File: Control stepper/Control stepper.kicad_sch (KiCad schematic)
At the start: 3 parts, among them Q1 2n2222a

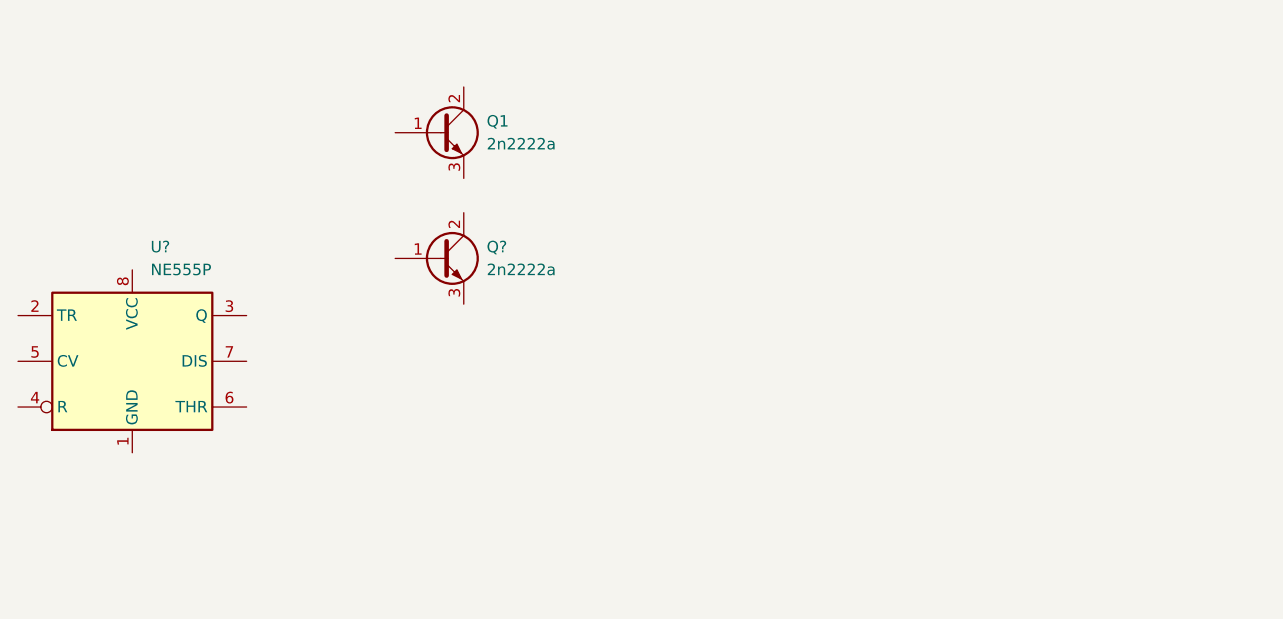
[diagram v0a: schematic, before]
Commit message: Añadida carpeta de código de arduino
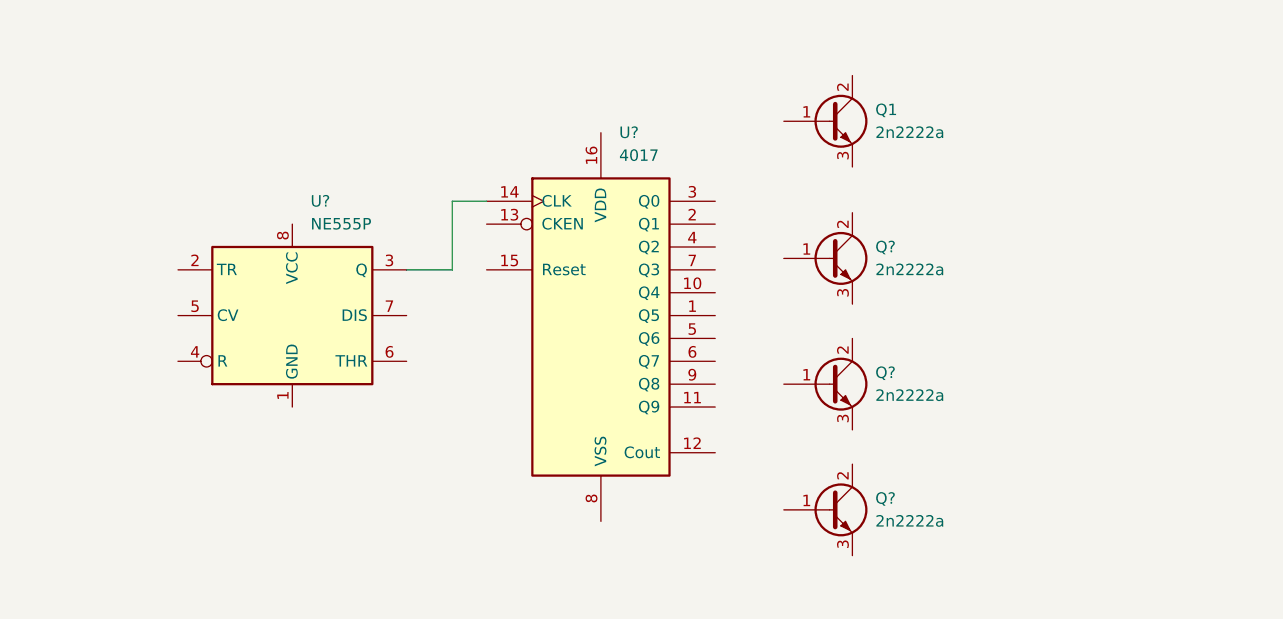
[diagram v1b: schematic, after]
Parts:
- added Q? (x2): 2n2222a, Package_TO_SOT_THT:TO-3PB-3_Vertical, symbol Transistor_BJT:2SD1047
- added U?: 4017, symbol 4xxx:4017
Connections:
- net at U?.3 (Q): now also U?.14 (CLK)
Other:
- moved on the sheet: Q1, Q?, U?
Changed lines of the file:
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@@
 (kicad_sch (version 20211123) (generator eeschema)
   (paper "A4")
-  (symbol (lib_id "Timer:NE555P") (at 64.77 109.22 0) (unit 1)
+  (wire (pts (xy 100.33 99.06) (xy 100.33 91.44))
+    (stroke (width 0) (type default) (color 0 0 0 0))
+  )
+  (wire (pts (xy 100.33 91.44) (xy 104.14 91.44))
+    (stroke (width 0) (type default) (color 0 0 0 0))
+  )
+  (wire (pts (xy 95.25 99.06) (xy 100.33 99.06))
+    (stroke (width 0) (type default) (color 0 0 0 0))
+  )
+  (symbol (lib_id "Timer:NE555P") (at 82.55 104.14 0) (unit 1)
     (in_bom yes) (on_board yes) (fields_autoplaced)
-    (property "Reference" "U?" (id 0) (at 66.7894 96.52 0)
+    (property "Reference" "U?" (id 0) (at 84.5694 91.44 0)
       (effects (font (size 1.27 1.27)) (justify left))
     )
-    (property "Value" "NE555P" (id 1) (at 66.7894 99.06 0)
+    (property "Value" "NE555P" (id 1) (at 84.5694 93.98 0)
       (effects (font (size 1.27 1.27)) (justify left))
     )
-    (property "Footprint" "Package_DIP:DIP-8_W7.62mm" (id 2) (at 81.28 119.38 0)
+    (property "Footprint" "Package_DIP:DIP-8_W7.62mm" (id 2) (at 99.06 114.3 0)
       (effects (font (size 1.27 1.27)) hide)
     )
-    (property "Datasheet" "http://www.ti.com/lit/ds/symlink/ne555.pdf" (id 3) (at 86.36 119.38 0)
+    (property "Datasheet" "http://www.ti.com/lit/ds/symlink/ne555.pdf" (id 3) (at 104.14 114.3 0)
       (effects (font (size 1.27 1.27)) hide)
     )
@@
     (pin "7")
   )
-  (symbol (lib_id "Transistor_BJT:2SD1047") (at 99.06 97.79 0) (unit 1)
+  (symbol (lib_id "Transistor_BJT:2SD1047") (at 142.24 111.76 0) (unit 1)
     (in_bom yes) (on_board yes) (fields_autoplaced)
-    (property "Reference" "Q?" (id 0) (at 104.14 96.5199 0)
+    (property "Reference" "Q?" (id 0) (at 147.32 110.4899 0)
       (effects (font (size 1.27 1.27)) (justify left))
     )
-    (property "Value" "2n2222a" (id 1) (at 104.14 99.0599 0)
+    (property "Value" "2n2222a" (id 1) (at 147.32 113.0299 0)
       (effects (font (size 1.27 1.27)) (justify left))
     )
-    (property "Footprint" "Package_TO_SOT_THT:TO-3PB-3_Vertical" (id 2) (at 105.41 99.695 0)
+    (property "Footprint" "Package_TO_SOT_THT:TO-3PB-3_Vertical" (id 2) (at 148.59 113.665 0)
       (effects (font (size 1.27 1.27) italic) (justify left) hide)
     )
-    (property "Datasheet" "http://www.st.com/resource/en/datasheet/2sd1047.pdf" (id 3) (at 99.06 97.79 0)
+    (property "Datasheet" "http://www.st.com/resource/en/datasheet/2sd1047.pdf" (id 3) (at 142.24 111.76 0)
       (effects (font (size 1.27 1.27)) (justify left) hide)
     )
@@
     (pin "3")
   )
-  (symbol (lib_id "Transistor_BJT:2SD1047") (at 99.06 83.82 0) (unit 1)
+  (symbol (lib_id "Transistor_BJT:2SD1047") (at 142.24 125.73 0) (unit 1)
     (in_bom yes) (on_board yes) (fields_autoplaced)
-    (property "Reference" "Q1" (id 0) (at 104.14 82.5499 0)
+    (property "Reference" "Q?" (id 0) (at 147.32 124.4599 0)
       (effects (font (size 1.27 1.27)) (justify left))
     )
-    (property "Value" "2n2222a" (id 1) (at 104.14 85.0899 0)
+    (property "Value" "2n2222a" (id 1) (at 147.32 126.9999 0)
       (effects (font (size 1.27 1.27)) (justify left))
     )
-    (property "Footprint" "Package_TO_SOT_THT:TO-3PB-3_Vertical" (id 2) (at 105.41 85.725 0)
+    (property "Footprint" "Package_TO_SOT_THT:TO-3PB-3_Vertical" (id 2) (at 148.59 127.635 0)
       (effects (font (size 1.27 1.27) italic) (justify left) hide)
     )
-    (property "Datasheet" "http://www.st.com/resource/en/datasheet/2sd1047.pdf" (id 3) (at 99.06 83.82 0)
+    (property "Datasheet" "http://www.st.com/resource/en/datasheet/2sd1047.pdf" (id 3) (at 142.24 125.73 0)
       (effects (font (size 1.27 1.27)) (justify left) hide)
     )
@@
     (pin "2")
     (pin "3")
+  )
+  (symbol (lib_id "Transistor_BJT:2SD1047") (at 142.24 97.79 0) (unit 1)
+    (in_bom yes) (on_board yes) (fields_autoplaced)
+    (property "Reference" "Q?" (id 0) (at 147.32 96.5199 0)
+      (effects (font (size 1.27 1.27)) (justify left))
+    )
+    (property "Value" "2n2222a" (id 1) (at 147.32 99.0599 0)
+      (effects (font (size 1.27 1.27)) (justify left))
+    )
+    (property "Footprint" "Package_TO_SOT_THT:TO-3PB-3_Vertical" (id 2) (at 148.59 99.695 0)
+      (effects (font (size 1.27 1.27) italic) (justify left) hide)
+    )
+    (property "Datasheet" "http://www.st.com/resource/en/datasheet/2sd1047.pdf" (id 3) (at 142.24 97.79 0)
+      (effects (font (size 1.27 1.27)) (justify left) hide)
+    )
+    (pin "1")
+    (pin "2")
+    (pin "3")
+  )
+  (symbol (lib_id "Transistor_BJT:2SD1047") (at 142.24 82.55 0) (unit 1)
+    (in_bom yes) (on_board yes) (fields_autoplaced)
+    (property "Reference" "Q1" (id 0) (at 147.32 81.2799 0)
+      (effects (font (size 1.27 1.27)) (justify left))
+    )
+    (property "Value" "2n2222a" (id 1) (at 147.32 83.8199 0)
+      (effects (font (size 1.27 1.27)) (justify left))
+    )
+    (property "Footprint" "Package_TO_SOT_THT:TO-3PB-3_Vertical" (id 2) (at 148.59 84.455 0)
+      (effects (font (size 1.27 1.27) italic) (justify left) hide)
+    )
+    (property "Datasheet" "http://www.st.com/resource/en/datasheet/2sd1047.pdf" (id 3) (at 142.24 82.55 0)
+      (effects (font (size 1.27 1.27)) (justify left) hide)
+    )
+    (pin "1")
+    (pin "2")
+    (pin "3")
+  )
+  (symbol (lib_id "4xxx:4017") (at 116.84 104.14 0) (unit 1)
+    (in_bom yes) (on_board yes) (fields_autoplaced)
+    (property "Reference" "U?" (id 0) (at 118.8594 83.82 0)
+      (effects (font (size 1.27 1.27)) (justify left))
+    )
+    (property "Value" "4017" (id 1) (at 118.8594 86.36 0)
+      (effects (font (size 1.27 1.27)) (justify left))
+    )
+    (property "Footprint" "" (id 2) (at 116.84 104.14 0)
+      (effects (font (size 1.27 1.27)) hide)
+    )
+    (property "Datasheet" "http://www.intersil.com/content/dam/Intersil/documents/cd40/cd4017bms-22bms.pdf" (id 3) (at 116.84 104.14 0)
+      (effects (font (size 1.27 1.27)) hide)
+    )
+    (pin "1")
+    (pin "10")
+    (pin "11")
+    (pin "12")
+    (pin "13")
+    (pin "14")
+    (pin "15")
+    (pin "16")
+    (pin "2")
+    (pin "3")
+    (pin "4")
+    (pin "5")
+    (pin "6")
+    (pin "7")
+    (pin "8")
+    (pin "9")
   )
   (sheet_instances
@@
       (reference "Q1") (unit 1) (value "2n2222a") (footprint "Package_TO_SOT_THT:TO-3PB-3_Vertical")
     )
+    (path "/2ce3dcaa-64a4-4ec7-925e-cda34a695a36"
+      (reference "Q?") (unit 1) (value "2n2222a") (footprint "Package_TO_SOT_THT:TO-3PB-3_Vertical")
+    )
+    (path "/2eec7807-2036-42a0-b763-d8d7931d6a94"
+      (reference "Q?") (unit 1) (value "2n2222a") (footprint "Package_TO_SOT_THT:TO-3PB-3_Vertical")
+    )
     (path "/383e22ae-7025-40ad-b4cf-dc8861149b49"
       (reference "Q?") (unit 1) (value "2n2222a") (footprint "Package_TO_SOT_THT:TO-3PB-3_Vertical")
@@
       (reference "U?") (unit 1) (value "NE555P") (footprint "Package_DIP:DIP-8_W7.62mm")
     )
+    (path "/97b177ea-de0c-48c8-bcee-9dde2dbdcc6f"
+      (reference "U?") (unit 1) (value "4017") (footprint "")
+    )
   )

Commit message: Terminado esquemático del stepper,falta el generador de pulsos
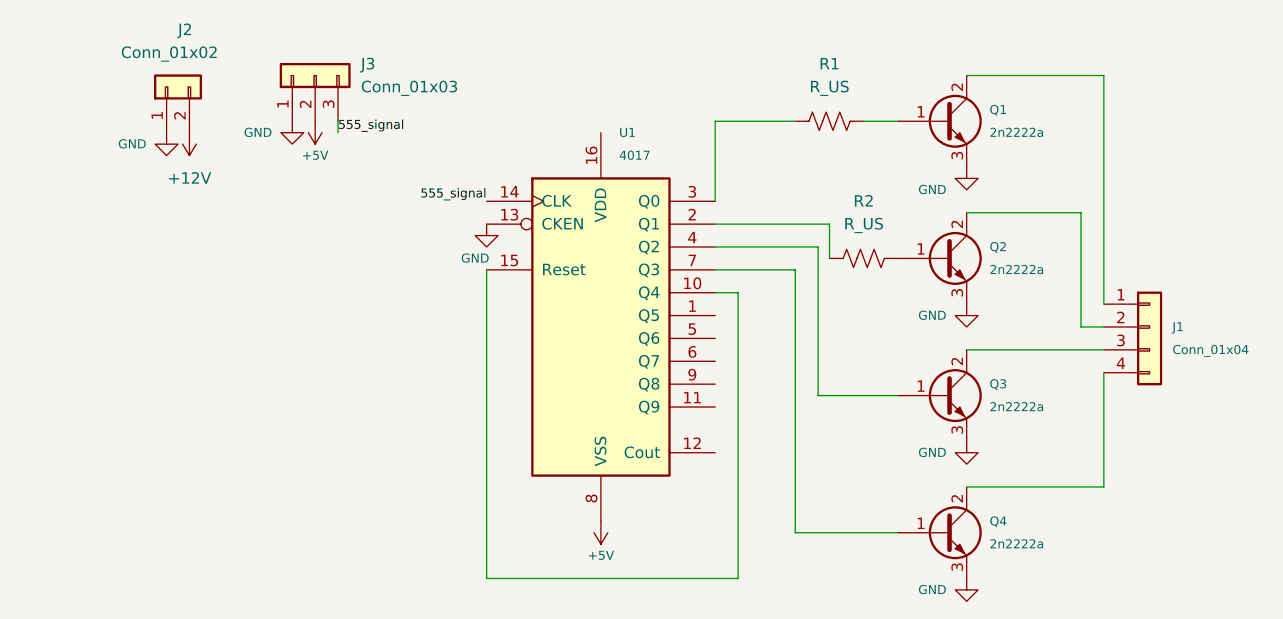
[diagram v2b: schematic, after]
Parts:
- removed U?: NE555P, Package_DIP:DIP-8_W7.62mm, symbol Timer:NE555P
- added J1: Conn_01x04, TerminalBlock:TerminalBlock_bornier-4_P5.08mm, symbol Connector_Generic:Conn_01x04
- added J2: Conn_01x02, TerminalBlock:TerminalBlock_bornier-2_P5.08mm, symbol Connector_Generic:Conn_01x02
- added J3: Conn_01x03, TerminalBlock:TerminalBlock_bornier-3_P5.08mm, symbol Connector_Generic:Conn_01x03
- added R1, R2: R_US, Resistor_THT:R_Axial_DIN0207_L6.3mm_D2.5mm_P15.24mm_Horizontal, symbol Device:R_US
- U1: renamed from U?; footprint (none) -> Package_DIP:DIP-16_W7.62mm_Socket_LongPads
- gave numbers to parts that had none: 3
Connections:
- net 555_signal: now reaches U1.14 (CLK)
- net 555_signal: now also J3.3 (Pin_3)
- net at Q3.1 (B): now also U1.4 (Q2)
- net at Q3.2 (C): now also J1.3 (Pin_3)
- net GND: now reaches Q3.3 (E)
- net GND: now also Q1.3 (E), Q2.3 (E), Q4.3 (E), U1.13 (CKEN), J2.1 (Pin_1), J3.1 (Pin_1)
- net at Q4.1 (B): now also U1.7 (Q3)
- net at Q4.2 (C): now also J1.4 (Pin_4)
- net at Q2.1 (B): now also R2.1
- net at Q2.2 (C): now also J1.2 (Pin_2)
- net at Q1.1 (B): now also R1.1
- net at Q1.2 (C): now also J1.1 (Pin_1)
- net at U1.10 (Q4): now also U1.15 (Reset)
- net at U1.2 (Q1): now also R2.2
- net at U1.3 (Q0): now also R1.2
- net +5V: now reaches U1.8 (VSS)
- net +5V: now also J3.2 (Pin_2)
- new net +12V: J2.2 (Pin_2)
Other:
- moved on the sheet: Q1, Q2, Q3, Q4

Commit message: 3D casi completo falta la pata de abajo
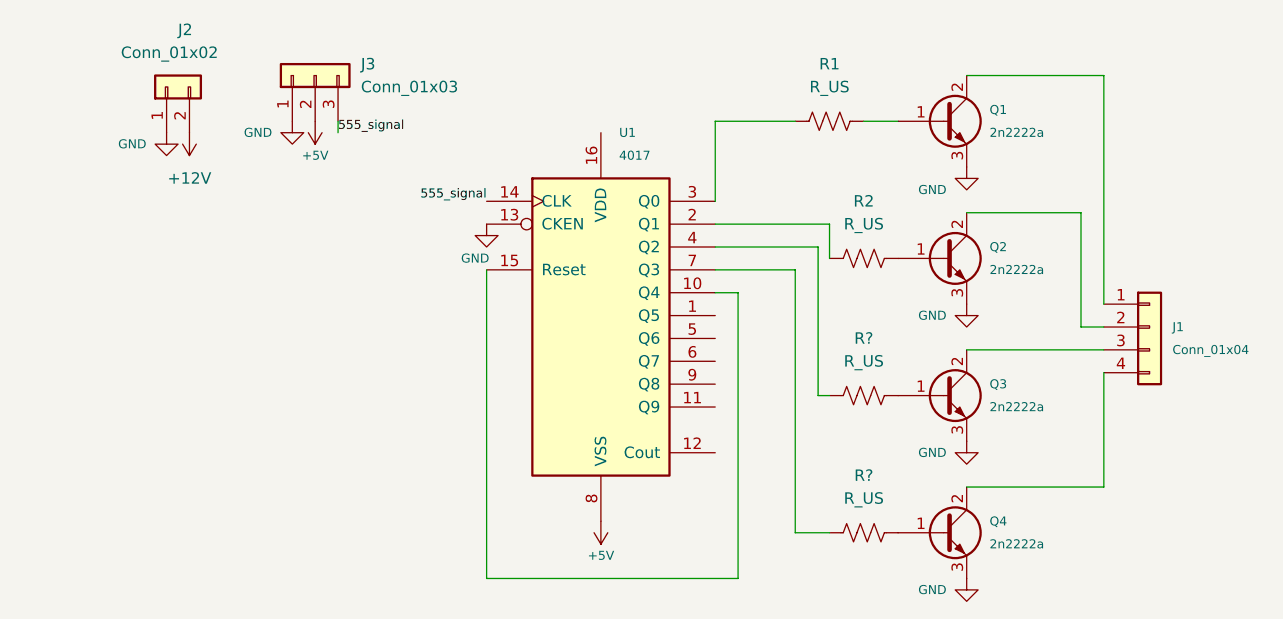
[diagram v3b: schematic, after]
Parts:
- added R? (x2): R_US, Resistor_THT:R_Axial_DIN0207_L6.3mm_D2.5mm_P15.24mm_Horizontal, symbol Device:R_US
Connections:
- net at Q3.1 (B): now also R?.1; no longer U1.4 (Q2)
- net at Q4.1 (B): now also R?.1; no longer U1.7 (Q3)
- new net: R?.2, U1.7 (Q3)
- new net: R?.2, U1.4 (Q2)
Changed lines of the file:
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@@
     (stroke (width 0) (type default) (color 0 0 0 0))
   )
-  (wire (pts (xy 140.97 113.03) (xy 149.86 113.03))
+  (wire (pts (xy 140.97 113.03) (xy 142.24 113.03))
     (stroke (width 0) (type default) (color 0 0 0 0))
   )
@@
     (stroke (width 0) (type default) (color 0 0 0 0))
   )
-  (wire (pts (xy 138.43 128.27) (xy 149.86 128.27))
-    (stroke (width 0) (type default) (color 0 0 0 0))
-  )
   (wire (pts (xy 129.54 93.98) (xy 142.24 93.98))
+    (stroke (width 0) (type default) (color 0 0 0 0))
+  )
+  (wire (pts (xy 138.43 128.27) (xy 142.24 128.27))
     (stroke (width 0) (type default) (color 0 0 0 0))
   )
@@
     (pin "4")
   )
+  (symbol (lib_id "Device:R_US") (at 146.05 128.27 270) (unit 1)
+    (in_bom yes) (on_board yes) (fields_autoplaced)
+    (property "Reference" "R?" (id 0) (at 146.05 121.92 90))
+    (property "Value" "R_US" (id 1) (at 146.05 124.46 90))
+    (property "Footprint" "Resistor_THT:R_Axial_DIN0207_L6.3mm_D2.5mm_P15.24mm_Horizontal" (id 2) (at 145.796 129.286 90)
+      (effects (font (size 1.27 1.27)) hide)
+    )
+    (property "Datasheet" "~" (id 3) (at 146.05 128.27 0)
+      (effects (font (size 1.27 1.27)) hide)
+    )
+    (pin "1")
+    (pin "2")
+  )
   (symbol (lib_id "power:+5V") (at 85.09 82.55 180) (unit 1)
     (in_bom yes) (on_board yes)
@@
     )
     (pin "1")
+  )
+  (symbol (lib_id "Device:R_US") (at 146.05 113.03 270) (unit 1)
+    (in_bom yes) (on_board yes) (fields_autoplaced)
+    (property "Reference" "R?" (id 0) (at 146.05 106.68 90))
+    (property "Value" "R_US" (id 1) (at 146.05 109.22 90))
+    (property "Footprint" "Resistor_THT:R_Axial_DIN0207_L6.3mm_D2.5mm_P15.24mm_Horizontal" (id 2) (at 145.796 114.046 90)
+      (effects (font (size 1.27 1.27)) hide)
+    )
+    (property "Datasheet" "~" (id 3) (at 146.05 113.03 0)
+      (effects (font (size 1.27 1.27)) hide)
+    )
+    (pin "1")
+    (pin "2")
   )
   (symbol (lib_id "Transistor_BJT:2SD1047") (at 154.94 82.55 0) (unit 1)
@@
       (reference "R2") (unit 1) (value "R_US") (footprint "Resistor_THT:R_Axial_DIN0207_L6.3mm_D2.5mm_P15.24mm_Horizontal")
     )
+    (path "/596de77e-eba4-4422-9d2c-ada9bb20e388"
+      (reference "R?") (unit 1) (value "R_US") (footprint "Resistor_THT:R_Axial_DIN0207_L6.3mm_D2.5mm_P15.24mm_Horizontal")
+    )
+    (path "/643fd6ba-3850-49de-aa16-31998639be17"
+      (reference "R?") (unit 1) (value "R_US") (footprint "Resistor_THT:R_Axial_DIN0207_L6.3mm_D2.5mm_P15.24mm_Horizontal")
+    )
     (path "/97b177ea-de0c-48c8-bcee-9dde2dbdcc6f"
